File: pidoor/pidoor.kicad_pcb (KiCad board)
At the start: 2 copper layers, 50 x 28 mm, 38 parts, among them P1 PI, P2 PWR, P3 IN0, P4 IN1, P5 IN2, P6 IN3, P7 READER, P8 MAG0, P9 MAG1, Q1 PMN25UN, Q2 PMN25UN, Q3 PMN25UN, Q4 PMN25UN, U1 MAX232, U2 3.3v

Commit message: v0.0.1
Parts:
- removed C11: 1µ, Capacitors_SMD:C_0603_HandSoldering
- removed P8: MAG0, pidoor:3_5mm_terminal_1x04
- removed P9: MAG1, pidoor:3_5mm_terminal_1x04
- removed Q4: PMN25UN, TO_SOT_Packages_SMD:SC-70-6_Handsoldering
- removed R11: 1k, Resistors_SMD:R_0603_HandSoldering
- removed R12: 100, Resistors_SMD:R_0603_HandSoldering
- C1, C10, C2, C3, C4, C5, C6, C7, C8, C9: footprint Capacitors_SMD:C_0603_HandSoldering -> Capacitors_SMD:C_0603
- P1: footprint pin_array_13x2 -> Socket_Strips:Socket_Strip_Straight_2x13; moved to B.Cu
- P6: value IN3 -> READER; footprint pidoor:3_5mm_terminal_1x02 -> pidoor:3_5mm_terminal_1x05; moved to B.Cu
- P7: value READER -> MAG; footprint pidoor:3_5mm_terminal_1x05 -> pidoor:3_5mm_terminal_1x04
- Q1: footprint TO_SOT_Packages_SMD:SC-70-6_Handsoldering -> TO_SOT_Packages_SMD:SOT-23; moved to B.Cu
- Q2, Q3: footprint TO_SOT_Packages_SMD:SC-70-6_Handsoldering -> TO_SOT_Packages_SMD:SOT-23
- R1: footprint Resistors_SMD:R_0603_HandSoldering -> Resistors_SMD:R_0603
- R10, R9: value 100 -> 4k7; footprint Resistors_SMD:R_0603_HandSoldering -> Resistors_SMD:R_0603
- R2: value 1k -> 4K7; footprint Resistors_SMD:R_0603_HandSoldering -> Resistors_SMD:R_0603
- R3: value 100 -> 4K7; footprint Resistors_SMD:R_0603_HandSoldering -> Resistors_SMD:R_0603
- R4, R6, R8: value 4K7 -> 4k7; footprint Resistors_SMD:R_0603_HandSoldering -> Resistors_SMD:R_0603
- R5, R7: value 1k -> 4k7; footprint Resistors_SMD:R_0603_HandSoldering -> Resistors_SMD:R_0603
- U1: value MAX232 -> 3.3v; footprint Housings_SOIC:SOIC-16_3.9x9.9mm_Pitch1.27mm -> pidoor:MIC5317
- U2: value 3.3v -> MAX232; footprint TO_SOT_Packages_SMD:SOT-23-5 -> Housings_SOIC:SOIC-16_3.9x9.9mm_Pitch1.27mm
- moved C8 39.6 mm to (175.8, 138.3), turned to 90 degrees
- moved C7 37.2 mm to (172.8, 141.3)
- moved R3 31.1 mm to (137.8, 135.8), turned to 180 degrees
- moved U2 27.4 mm to (169.3, 136.3), turned to 90 degrees
- moved C9 26.9 mm to (169.3, 141.3), turned to 180 degrees
- moved R7 23.1 mm to (155.1, 124.8), turned to 90 degrees
- moved C6 22.6 mm to (175.8, 134.3), turned to 90 degrees
- moved P6 20.5 mm to (144.0, 119.5), turned to 90 degrees
- moved Q3 18.5 mm to (165.3, 124.5), turned to 270 degrees
- moved Q1 17.5 mm to (152.1, 124.5), turned to 270 degrees
- moved P7 17.3 mm to (160.9, 119.5)
- moved C5 15.4 mm to (137.8, 139.8), turned to 180 degrees
- moved P1 15.3 mm to (145.8, 130.3)
- moved R10 15.1 mm to (162.3, 123.8), turned to 270 degrees
- moved C2 13.4 mm to (141.8, 131.8), turned to 0 degrees
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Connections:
- C1 pad 1: Net-(C1-Pad1) -> +5V
- C1 pad 2: Net-(C1-Pad2) -> GND
- C10 pad 1: /GPIO22 -> GND
- C10 pad 2: GND -> Net-(C10-Pad2)
- C2 pad 1: Net-(C2-Pad1) -> +3V3
- C2 pad 2: Net-(C2-Pad2) -> GND
- C3 pad 1: /GPIO4 -> /IN0
- C4 pad 1: GND -> /IN1
- C4 pad 2: +5V -> GND
- C5 pad 1: GND -> /IN2
- C5 pad 2: Net-(C5-Pad2) -> GND
- C6 pad 2: Net-(C6-Pad2) -> +5V
- C7 pad 1: /GPIO17 -> Net-(C7-Pad1)
- C7 pad 2: GND -> Net-(C7-Pad2)
- C8 pad 1: /GPIO21 -> GND
- C8 pad 2: GND -> Net-(C8-Pad2)
- C9 pad 1: +5V -> Net-(C9-Pad1)
- C9 pad 2: GND -> Net-(C9-Pad2)
- P1 pad 1: Net-(P1-Pad1) -> (no net)
- P1 pad 11: /GPIO17 -> /EMG
- P1 pad 12: /GPIO18 -> /BUZZER
- P1 pad 13: /GPIO21 -> (no net)
- P1 pad 14: Net-(P1-Pad14) -> GND
- P1 pad 15: /GPIO22 -> (no net)
- P1 pad 16: /GPIO23 -> /EN_READ
- P1 pad 17: Net-(P1-Pad17) -> (no net)
- P1 pad 18: /GPIO24 -> /MAG
- P1 pad 19: Net-(P1-Pad19) -> (no net)
- P1 pad 20: Net-(P1-Pad20) -> GND
- P1 pad 21: Net-(P1-Pad21) -> (no net)
- P1 pad 22: /GPIO25 -> (no net)
- P1 pad 23: Net-(P1-Pad23) -> (no net)
- P1 pad 24: Net-(P1-Pad24) -> (no net)
- P1 pad 25: Net-(P1-Pad25) -> GND
- P1 pad 26: Net-(P1-Pad26) -> (no net)
- P1 pad 3: Net-(P1-Pad3) -> /IN2
- P1 pad 4: Net-(P1-Pad4) -> +5V
- P1 pad 5: Net-(P1-Pad5) -> /IN1
- P1 pad 7: /GPIO4 -> /IN0
- P1 pad 9: Net-(P1-Pad9) -> GND
- P6 pad 1: GND -> Net-(P6-Pad1)
- P7 pad 2: Net-(P7-Pad2) -> /12_EMG
- P7 pad 3: /EIA-TX -> /12_EMG
- P7 pad 4: /EIA-RX -> +12V
- Q1 pad 1: Net-(P8-Pad1) -> Net-(P6-Pad1)
- Q1 pad 2: /GPIO24 -> /EN_READ
- Q2 pad 1: Net-(P7-Pad1) -> Net-(P6-Pad2)
- Q2 pad 2: /GPIO23 -> /BUZZER
- Q3 pad 1: Net-(P9-Pad1) -> Net-(P7-Pad1)
- Q3 pad 2: /GPIO25 -> /MAG
- R10 pad 1: /GPIO25 -> /12_EMG
- R2 pad 1: /GPIO4 -> +3V3
- R2 pad 2: Net-(P3-Pad2) -> Net-(P4-Pad2)
- R3 pad 1: /GPIO24 -> +3V3
- R3 pad 2: GND -> Net-(P5-Pad2)
- R4 pad 1: +3V3 -> /IN0
- R4 pad 2: Net-(P4-Pad2) -> Net-(P3-Pad2)
- R5 pad 1: /GPIO17 -> /IN1
- R6 pad 1: +3V3 -> /IN2
- R7 pad 1: /GPIO21 -> /EN_READ
- R7 pad 2: Net-(P5-Pad2) -> GND
- R8 pad 1: +3V3 -> /BUZZER
- R8 pad 2: Net-(P6-Pad2) -> GND
- R9 pad 1: /GPIO23 -> /MAG
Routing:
- net +5V: track 0.00 -> 81.7 mm
- net +12V: track 115.7 -> 39.8 mm
- net /IN0: track 0.00 -> 50.5 mm
- net /EIA-TX: track 0.00 -> 49.8 mm
- net /EIA-RX: track 0.00 -> 42.2 mm
- net /IN1: track 0.00 -> 40.7 mm
- net /12_EMG: track 0.00 -> 33.3 mm, vias 0 -> 1
- net /TXD: track 0.00 -> 19.2 mm
- net +3V3: track 0.00 -> 17.4 mm
- net /RXD: track 0.00 -> 16.7 mm
- net /IN2: track 0.00 -> 15.7 mm
- net /GPIO25: track 13.5 -> 0.00 mm
- net /BUZZER: track 0.00 -> 12.4 mm
- net /EN_READ: track 0.00 -> 11.8 mm
- net /EMG: track 0.00 -> 8.71 mm
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- added copper zone on F.Cu, net GND
- removed copper zone on F.Cu, net +3V3
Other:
- net class Default: via_dia 0.9 -> 1
- net class Power: trace_width 0.5 -> 1
- board text added: "+"
- board text added: "BZ"
- board text added: "EMG"
- board text added: "EN"
- board text added: "GND"
- board text added: "IN0"
- board text added: "IN1"
- board text added: "IN2"
- board text added: "MAG"
- board text added: "RX"
- board text added: "TX"

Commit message: RFID back
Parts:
- Q1, Q2, Q3: value PMN25UN -> PMV16XN
- moved Q2 0.25 mm to (146.3, 124.5), turned to 180 degrees
- turned Q1 to 180 degrees
- turned Q3 to 180 degrees
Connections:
- Q1 pad 1: Net-(P6-Pad1) -> /EN_READ
- Q1 pad 2: /EN_READ -> GND
- Q1 pad 3: GND -> Net-(P6-Pad1)
- Q2 pad 1: Net-(P6-Pad2) -> /BUZZER
- Q2 pad 2: /BUZZER -> GND
- Q2 pad 3: GND -> Net-(P6-Pad2)
- Q3 pad 1: Net-(P7-Pad1) -> /MAG
- Q3 pad 2: /MAG -> GND
- Q3 pad 3: GND -> Net-(P7-Pad1)
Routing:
- net Net-(P6-Pad2): track 4.25 -> 5.14 mm
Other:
- board text added: "PiDoor v0.2.0 ©2016"

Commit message: license
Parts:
- P1: value PI -> CONN_02X13
- U1: value 3.3v -> MIC5317-3.3YM5
- U2: value MAX232 -> ST232BDR
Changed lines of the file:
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@@
     (links 72)
     (no_connects 0)
-    (area 127.924999 114.924999 178.075001 143.075001)
+    (area 124.049999 106.325 242.964763 187.88)
     (thickness 1.6)
     (drawings 66)
@@
     (date 2016-09-29)
     (rev 0.2.0)
-    (company "Wirehive Ltd")
+    (company "©2016 Wirehive ltd, CC BY-SA ")
   )
   (layers
@@
       (effects (font (size 1.5 1.5) (thickness 0.25)) (justify mirror))
     )
-    (fp_text value PI (at 0 3.1) (layer B.Fab)
+    (fp_text value CONN_02X13 (at 0 3.1) (layer B.Fab)
       (effects (font (size 1.5 1.5) (thickness 0.25)) (justify mirror))
     )
@@
       (effects (font (size 1.5 1.5) (thickness 0.25)) (justify mirror))
     )
-    (fp_text value MAX232 (at 0 -6 90) (layer B.Fab)
+    (fp_text value ST232BDR (at 0 -6 90) (layer B.Fab)
       (effects (font (size 1.5 1.5) (thickness 0.25)) (justify mirror))
     )
@@
       (effects (font (size 1.5 1.5) (thickness 0.25)) (justify mirror))
     )
-    (fp_text value 3.3v (at -0.05 -2.35 270) (layer B.Fab)
-      (effects (font (size 1.5 1.5) (thickness 0.25)) (justify mirror))
-    )
+    (fp_text value MIC5317-3.3YM5 (at -0.05 -2.35 270) (layer B.Fab)
+      (effects (font (size 1.5 1.5) (thickness 0.25)) (justify mirror))
+    )

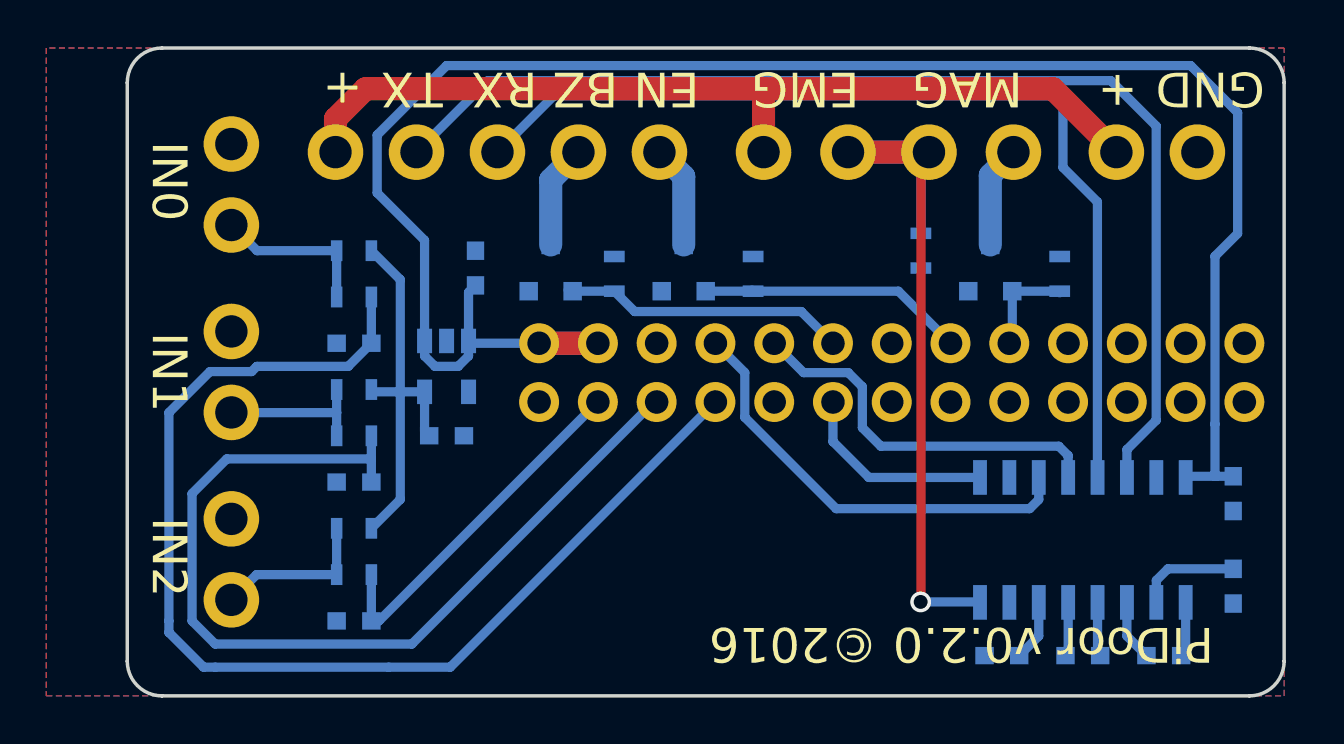
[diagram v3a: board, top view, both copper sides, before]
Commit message: Probably best if the level converters are connected to the correct level
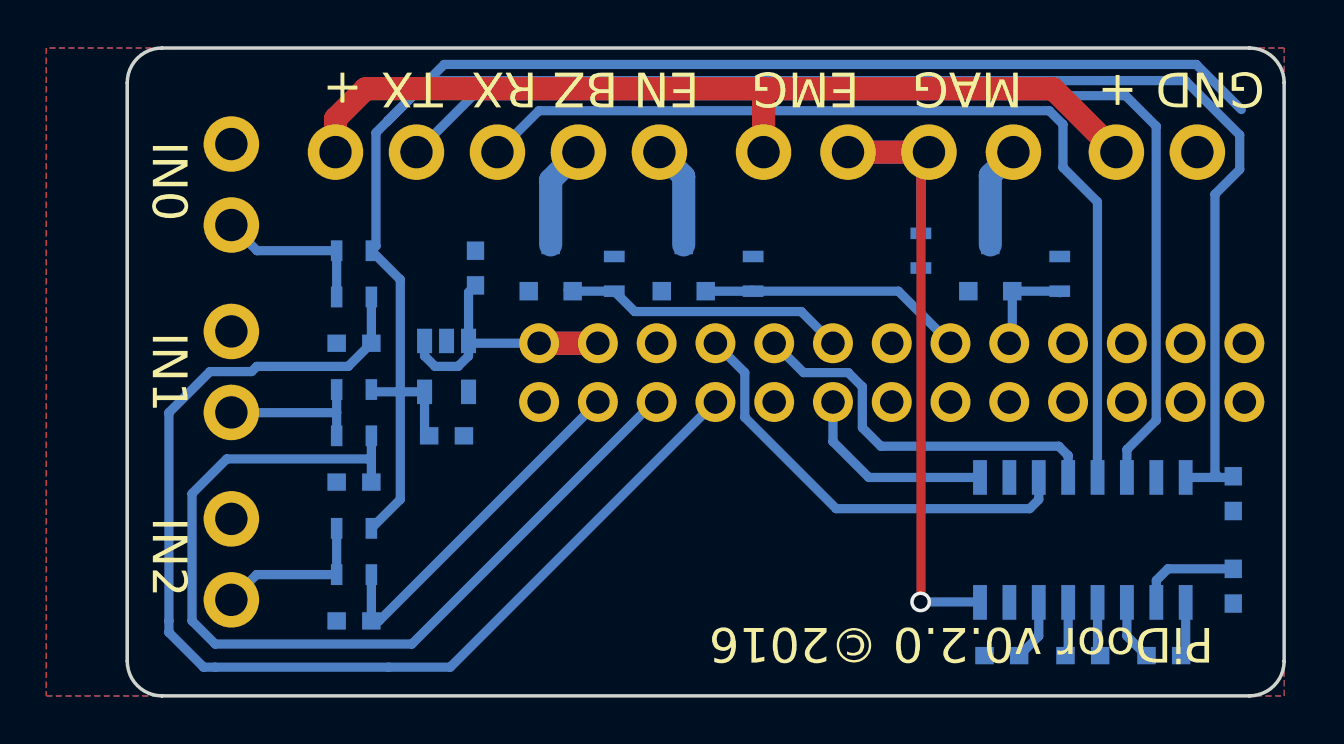
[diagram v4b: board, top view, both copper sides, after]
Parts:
- U2: value ST232BDR -> ST3232BDR
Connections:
- C6 pad 2: +5V -> +3V3
- U2 pad 16: +5V -> +3V3
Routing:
- net +3V3: track 17.4 -> 118.1 mm
- net +5V: track 81.7 -> 14.3 mm
- net /EIA-RX: track 42.2 -> 41.3 mm
- net /EIA-TX: track 49.8 -> 49.2 mm
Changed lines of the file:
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@@
     (links 72)
     (no_connects 0)
-    (area 124.049999 106.325 242.964763 187.88)
+    (area 127.924999 114.924999 178.075001 143.075001)
     (thickness 1.6)
     (drawings 66)
-    (tracks 162)
+    (tracks 165)
     (zones 0)
     (modules 32)
@@
       (net 2 GND))
     (pad 2 smd rect (at 0.75 0 90) (size 0.8 0.75) (layers B.Cu B.Paste B.Mask)
-      (net 1 +5V))
+      (net 3 +3V3))
     (model Capacitors_SMD.3dshapes/C_0603.wrl
       (at (xyz 0 0 0))
@@
       (effects (font (size 1.5 1.5) (thickness 0.25)) (justify mirror))
     )
-    (fp_text value ST232BDR (at 0 -6 90) (layer B.Fab)
+    (fp_text value ST3232BDR (at 0 -6 90) (layer B.Fab)
       (effects (font (size 1.5 1.5) (thickness 0.25)) (justify mirror))
     )
@@
       (net 2 GND))
     (pad 16 smd rect (at 2.7 4.445 90) (size 1.5 0.6) (layers B.Cu B.Paste B.Mask)
-      (net 1 +5V))
+      (net 3 +3V3))
     (model Housings_SOIC.3dshapes/SOIC-16_3.9x9.9mm_Pitch1.27mm.wrl
       (at (xyz 0 0 0))
@@
   (gr_line (start 143.5 181) (end 228.5 181) (angle 90) (layer Dwgs.User) (width 0.15))
   (gr_line (start 143.5 125) (end 143.5 181) (angle 90) (layer Dwgs.User) (width 0.15))
-  (segment (start 175.01 131.26) (end 175.01 133.51) (width 0.4) (layer B.Cu) (net 1))
-  (segment (start 175.01 133.51) (end 175.05 133.51) (width 0.4) (layer B.Cu) (net 1))
-  (segment (start 175.01 131.26) (end 175.01 124) (width 0.4) (layer B.Cu) (net 1))
-  (segment (start 140.85 123.31) (end 138.8 121.26) (width 0.4) (layer B.Cu) (net 1))
-  (segment (start 138.8 121.26) (end 138.8 118.76) (width 0.4) (layer B.Cu) (net 1))
-  (segment (start 138.8 118.76) (end 141.8 115.76) (width 0.4) (layer B.Cu) (net 1))
-  (segment (start 141.8 115.76) (end 173.96 115.76) (width 0.4) (layer B.Cu) (net 1))
-  (segment (start 175.99 123.02) (end 175.99 117.79) (width 0.4) (layer B.Cu) (net 1))
-  (segment (start 175.99 117.79) (end 173.96 115.76) (width 0.4) (layer B.Cu) (net 1))
-  (segment (start 140.85 127.66) (end 140.85 123.31) (width 0.4) (layer B.Cu) (net 1) (status 10))
-  (segment (start 175.01 124) (end 175.99 123.02) (width 0.4) (layer B.Cu) (net 1))
   (segment (start 148.34 127.76) (end 145.8 127.76) (width 1) (layer F.Cu) (net 1) (status 30))
-  (segment (start 173.745 133.56) (end 173.795 133.51) (width 0.4) (layer B.Cu) (net 1) (status 30))
-  (segment (start 173.795 133.51) (end 175.05 133.51) (width 0.4) (layer B.Cu) (net 1) (status 30))
-  (segment (start 175.05 133.51) (end 175.8 133.51) (width 0.4) (layer B.Cu) (net 1) (status 30))
-  (segment (start 173.745 133.415) (end 173.745 133.56) (width 0.4) (layer B.Cu) (net 1) (status 30))
   (segment (start 148.34 127.76) (end 145.8 127.76) (width 1) (layer B.Cu) (net 1) (status 30))
   (segment (start 140.85 127.66) (end 140.85 128.31) (width 0.4) (layer B.Cu) (net 1) (status 10))
@@
   (segment (start 142.75 127.66) (end 142.85 127.76) (width 0.4) (layer B.Cu) (net 1) (status 30))
   (segment (start 142.85 127.76) (end 145.8 127.76) (width 0.4) (layer B.Cu) (net 1) (status 30))
+  (segment (start 139.25 118.16) (end 141 116.41) (width 0.4) (layer B.Cu) (net 3))
+  (segment (start 175.01 133.39) (end 175.18 133.56) (width 0.4) (layer B.Cu) (net 3))
+  (segment (start 175.01 121.32) (end 175.01 133.39) (width 0.4) (layer B.Cu) (net 3))
+  (segment (start 176.08 120.25) (end 175.01 121.32) (width 0.4) (layer B.Cu) (net 3))
+  (segment (start 176.08 118.76) (end 176.08 120.25) (width 0.4) (layer B.Cu) (net 3))
+  (segment (start 173.73 116.41) (end 176.08 118.76) (width 0.4) (layer B.Cu) (net 3))
+  (segment (start 141 116.41) (end 173.73 116.41) (width 0.4) (layer B.Cu) (net 3))
+  (segment (start 138.55 123.76) (end 138.75 123.56) (width 0.4) (layer B.Cu) (net 3))
+  (segment (start 138.75 123.56) (end 138.75 118.66) (width 0.4) (layer B.Cu) (net 3))
+  (segment (start 174.2 115.71) (end 176.15 117.66) (width 0.4) (layer B.Cu) (net 3))
+  (segment (start 141.7 115.71) (end 174.2 115.71) (width 0.4) (layer B.Cu) (net 3))
+  (segment (start 138.75 118.66) (end 139.25 118.16) (width 0.4) (layer B.Cu) (net 3))
+  (segment (start 139.25 118.16) (end 141.7 115.71) (width 0.4) (layer B.Cu) (net 3))
+  (segment (start 173.745 133.56) (end 175.18 133.56) (width 0.4) (layer B.Cu) (net 3))
+  (segment (start 175.18 133.56) (end 175.75 133.56) (width 0.4) (layer B.Cu) (net 3))
+  (segment (start 175.75 133.56) (end 175.8 133.51) (width 0.4) (layer B.Cu) (net 3))
+  (segment (start 173.745 133.56) (end 173.795 133.51) (width 0.4) (layer B.Cu) (net 3) (status 30))
+  (segment (start 173.745 133.415) (end 173.745 133.56) (width 0.4) (layer B.Cu) (net 3) (status 30))
   (segment (start 141.05 131.76) (end 140.85 131.56) (width 0.4) (layer B.Cu) (net 3) (status 30))
   (segment (start 140.85 131.56) (end 140.85 129.86) (width 0.4) (layer B.Cu) (net 3) (status 30))
@@
   (segment (start 168.665 132.615) (end 168.26 132.21) (width 0.4) (layer B.Cu) (net 18))
   (segment (start 168.65 133.545) (end 168.665 133.56) (width 0.4) (layer B.Cu) (net 18) (status 30))
-  (segment (start 146.43 117.07) (end 167.91 117.07) (width 0.4) (layer B.Cu) (net 19))
-  (segment (start 167.91 117.07) (end 168.44 117.6) (width 0.4) (layer B.Cu) (net 19))
-  (segment (start 168.44 117.6) (end 168.44 120.16) (width 0.4) (layer B.Cu) (net 19))
+  (segment (start 144 119.5) (end 145.79 117.71) (width 0.4) (layer B.Cu) (net 19))
+  (segment (start 167.85 117.71) (end 168.44 118.3) (width 0.4) (layer B.Cu) (net 19))
+  (segment (start 145.79 117.71) (end 167.85 117.71) (width 0.4) (layer B.Cu) (net 19))
+  (segment (start 168.44 118.3) (end 168.44 120.16) (width 0.4) (layer B.Cu) (net 19))
   (segment (start 169.93 121.65) (end 169.93 133.555) (width 0.4) (layer B.Cu) (net 19) (status 20))
   (segment (start 169.93 133.555) (end 169.935 133.56) (width 0.4) (layer B.Cu) (net 19) (status 30))
-  (segment (start 144 119.5) (end 146.43 117.07) (width 0.4) (layer B.Cu) (net 19) (status 10))
   (segment (start 168.44 120.16) (end 169.93 121.65) (width 0.4) (layer B.Cu) (net 19))
-  (segment (start 172.47 118.37) (end 172.47 131.09) (width 0.4) (layer B.Cu) (net 20))
+  (segment (start 140.5 119.5) (end 142.94 117.06) (width 0.4) (layer B.Cu) (net 20))
+  (segment (start 171.15 117.06) (end 172.47 118.38) (width 0.4) (layer B.Cu) (net 20))
+  (segment (start 142.94 117.06) (end 171.15 117.06) (width 0.4) (layer B.Cu) (net 20))
+  (segment (start 172.47 118.38) (end 172.47 131.09) (width 0.4) (layer B.Cu) (net 20))
   (segment (start 172.47 131.09) (end 171.205 132.355) (width 0.4) (layer B.Cu) (net 20))
   (segment (start 171.205 132.355) (end 171.205 133.56) (width 0.4) (layer B.Cu) (net 20) (status 20))
-  (segment (start 172.47 118.37) (end 170.51 116.41) (width 0.4) (layer B.Cu) (net 20))
-  (segment (start 170.51 116.41) (end 143.59 116.41) (width 0.4) (layer B.Cu) (net 20))
-  (segment (start 143.59 116.41) (end 140.5 119.5) (width 0.4) (layer B.Cu) (net 20) (status 20))
   (segment (start 129.8 139.76) (end 129.8 140.26) (width 0.4) (layer B.Cu) (net 21))
   (segment (start 129.8 130.76) (end 129.8 139.76) (width 0.4) (layer B.Cu) (net 21))

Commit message: relay for AC strikers
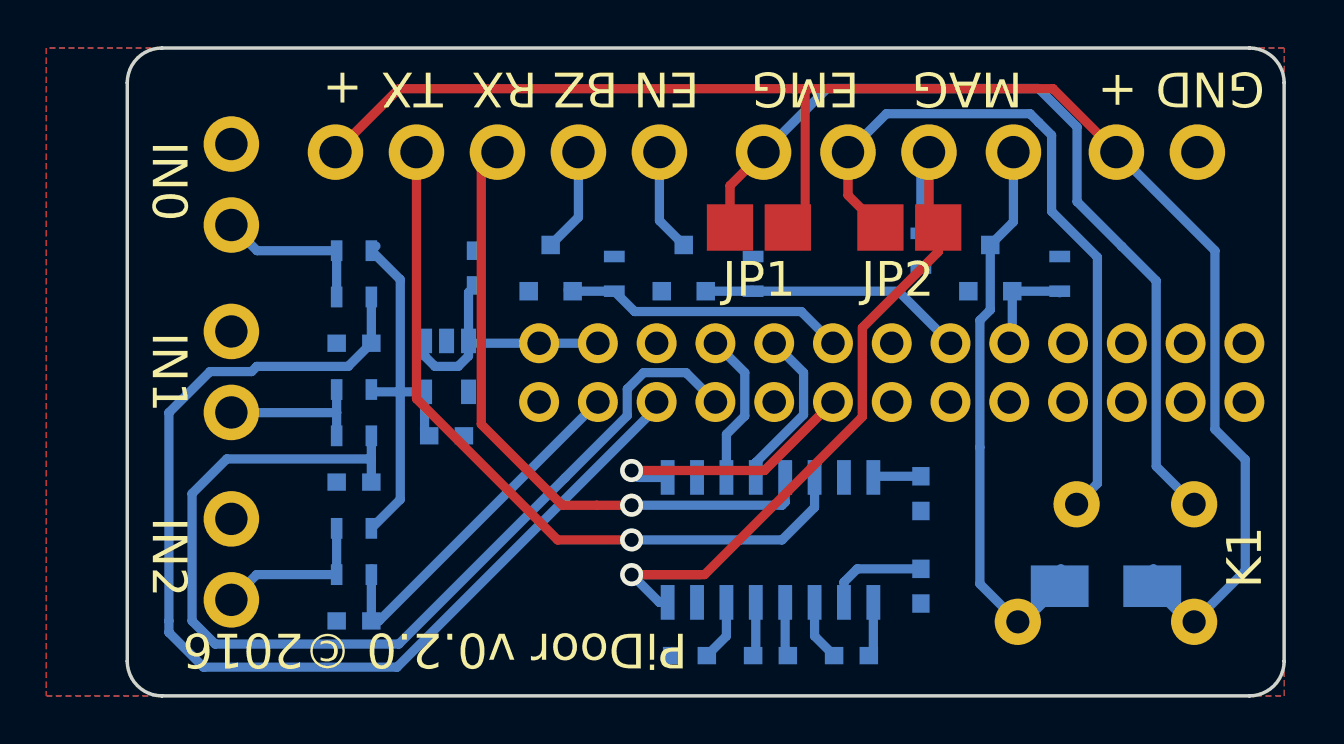
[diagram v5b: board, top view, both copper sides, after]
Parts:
- added D1: D_Small, Diodes_SMD:SMA_Standard, B.Cu at (170.3, 138.3)
- added JP1: JUMPER, pidoor:SMD_Jumper, F.Cu at (155.3, 122.8)
- added JP2: JUMPER, pidoor:SMD_Jumper, F.Cu at (161.8, 122.8)
- added K1: RELAY_G6L, pidoor:Relay_G6L, F.Cu at (170.3, 137.3)
- moved C10 13.5 mm to (152.3, 141.3)
- moved C6 13.5 mm to (162.3, 134.3)
- moved C7 13.5 mm to (159.3, 141.3)
- moved C8 13.5 mm to (162.3, 138.3)
- moved C9 13.5 mm to (155.8, 141.3)
- moved U2 13.5 mm to (155.8, 136.3)
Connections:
- P1 pad 5: /IN1 -> /IN0
- P1 pad 7: /IN0 -> /IN1
- P7 pad 3: /12_EMG -> Net-(JP2-Pad1)
- P7 pad 4: +12V -> Net-(JP1-Pad1)
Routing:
- net +3V3: track 118.1 -> 19.7 mm
- net Net-(JP1-Pad1): track 0.00 -> 37.6 mm
- net Net-(JP2-Pad1): track 0.00 -> 30.9 mm
- net +12V: track 39.8 -> 69.4 mm
- net Net-(D1-Pad2): track 4.43 -> 24.9 mm
- net /EIA-TX: track 49.2 -> 32.3 mm, vias 0 -> 1
- net /EIA-RX: track 41.3 -> 27.8 mm, vias 0 -> 1
- net /TXD: track 19.2 -> 6.66 mm
- net /RXD: track 16.7 -> 7.18 mm
- net /IN1: track 40.7 -> 45.0 mm
- net /EMG: track 8.71 -> 11.6 mm, vias 0 -> 1
- net +5V: track 14.3 -> 11.7 mm
- net /IN0: track 50.5 -> 48.2 mm
- net /12_EMG: track 33.8 -> 35.5 mm
- net Net-(P6-Pad2): track 5.14 -> 4.51 mm
